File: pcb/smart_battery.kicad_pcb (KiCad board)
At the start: 2 copper layers, 109.2 x 108 mm, 37 parts, among them J11 Conn_01x05_RTC, J12 Conn_HtrTh, J13 Conn_BattTh, Q1 MMBT5551L, Q2 MMBT5551L, U1 SPX3819M5-L-3-3, U10 FEATHER_M0_ADALOGGER, U11 FEATHERWING_HEATER_RELAY, U12 FEATHERWING_ETHERNET, U13 FEATHERWING_MINI_RELAY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

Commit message: Routed the new layout just need ground plane
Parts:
- added C5: C10uF, Capacitor_SMD:C_0805_2012Metric, B.Cu at (109.2, 74.9)
- added C6: C10uF, Capacitor_SMD:C_0805_2012Metric, B.Cu at (110.5, 90.2)
- added C7: C10uF, Capacitor_SMD:C_0805_2012Metric, B.Cu at (110.5, 92.7)
- added C8: C10nF, Capacitor_SMD:C_0805_2012Metric, B.Cu at (85.1, 30.5)
- added F1: Fuse_Small, Fuse:Fuseholder_Cylinder-5x20mm_Schurter_0031_8201_Horizontal_Open, B.Cu at (55.9, 82.5)
- added F2: Fuse_Small, Fuse:Fuseholder_Cylinder-5x20mm_Schurter_0031_8201_Horizontal_Open, B.Cu at (34.3, 55.9)
- added R10: 3.3K, Resistor_SMD:R_0805_2012Metric, B.Cu at (101.6, 52.1)
- added R11: R6.8k, Resistor_SMD:R_0805_2012Metric, B.Cu at (101.6, 54.6)
- added R12: 3.3K, Resistor_SMD:R_0805_2012Metric, B.Cu at (109.2, 72.4)
- added R13: R6.8k, Resistor_SMD:R_0805_2012Metric, B.Cu at (101.6, 95.2)
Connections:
- net /BATPWR renamed Net-(D1-Pad2)
- net /SOLPWR renamed Net-(D2-Pad2)
- C1 pad 1: /POUT -> +48V
- C2 pad 1: /Eth3.3 -> +48V
- C3 pad 1: /Eth3.3 -> +48V
- D1 pad 1: /DBPWR -> Net-(D1-Pad1)
- PS1 pad 1: Net-(D2-Pad1) -> +48V
- PS2 pad 2: /DBPWR -> +48V
- Q1 pad 3: /DBPWR -> +48V
- R5 pad 2: /POUT -> +48V
- R6 pad 1: /DBPWR -> +48V
- U1 pad 1: /POUT -> +48V
- U1 pad 5: /Eth3.3 -> +48V
- U12 pad P1_15: /Eth3.3 -> +48V
- U13 pad P1_1: GND -> Net-(U13-PadP1_1)
- U13 pad P1_13: GND -> Net-(U13-PadP1_1)
- U14 pad P2_2: /POUT -> +48V
- U1Batt1 pad 9: GND -> Net-(R12-Pad1)
- U2Solar1 pad 9: GND -> Net-(R10-Pad1)
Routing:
- net +48V: track 22.0 -> 274.3 mm
- net GND: track 551.9 -> 460.1 mm, vias 0 -> 7
- net /POUT: track 47.5 -> 0.00 mm, vias 1 -> 0
- net Net-(R12-Pad1): track 0.00 -> 39.2 mm
- net Net-(U13-PadP1_1): track 0.00 -> 36.4 mm
- net Net-(D1-Pad1): track 0.00 -> 32.6 mm
- net Net-(D2-Pad1): track 16.2 -> 46.5 mm
- net /DBPWR: track 27.2 -> 0.00 mm
- net /Eth3.3: track 19.2 -> 0.00 mm
- net /ENCS: track 119.3 -> 105.0 mm, vias 0 -> 1
- net Net-(R10-Pad1): track 0.00 -> 11.0 mm
- net +5V: track 195.5 -> 206.4 mm, vias 0 -> 1
- net Net-(D1-Pad2): track 49.0 -> 57.6 mm
- net /SUSET: track 43.2 -> 51.1 mm
- net /~RST: track 138.0 -> 144.7 mm
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- removed copper zone on F.Cu, net GND

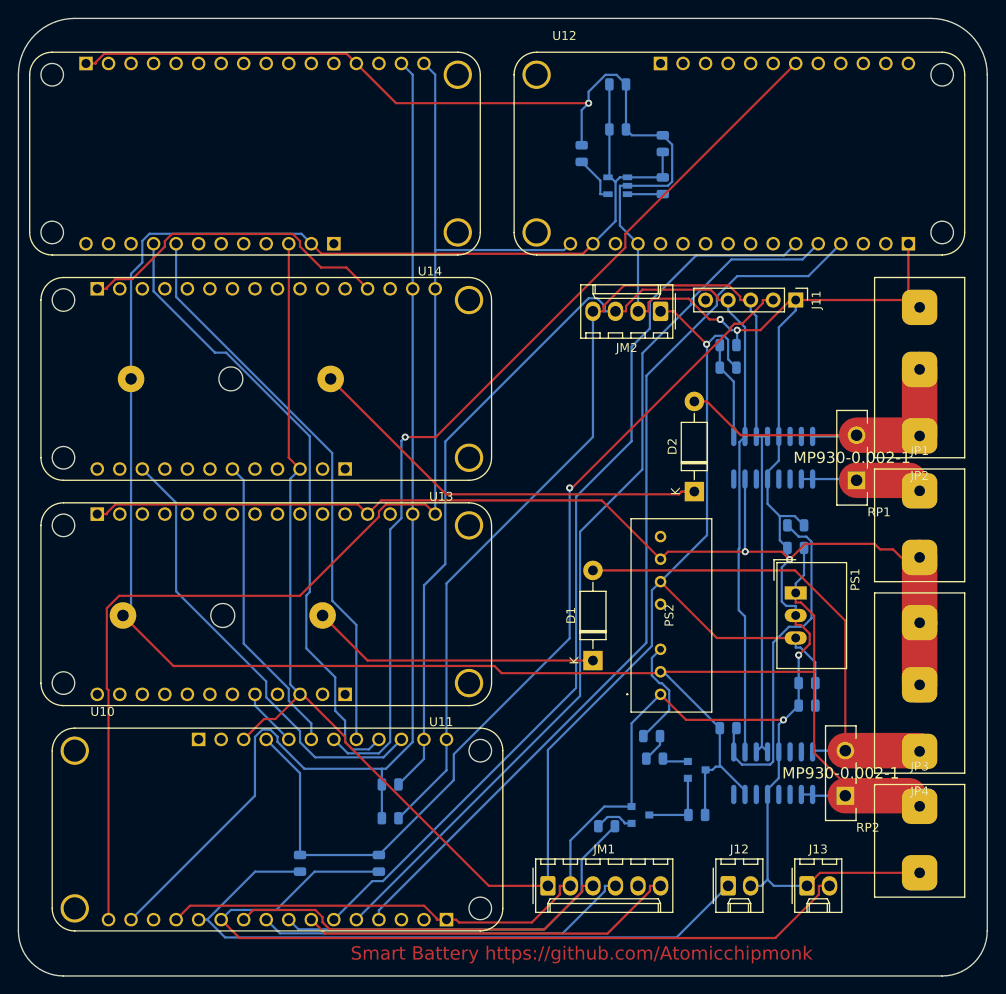
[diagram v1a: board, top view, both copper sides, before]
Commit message: Made the ground plane
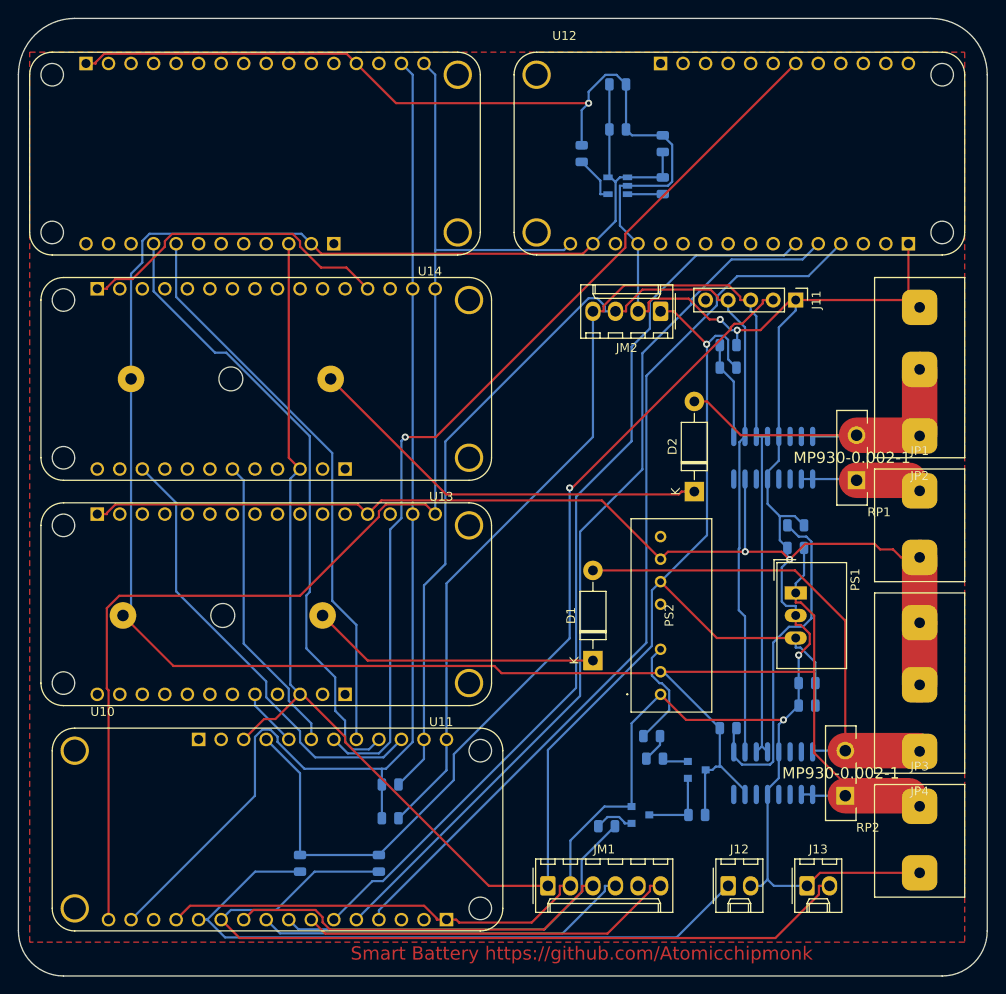
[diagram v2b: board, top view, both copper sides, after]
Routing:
- added copper zone on F.Cu, net GND
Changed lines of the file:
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@@
   (segment (start 32.5242 70.0297) (end 31.5703 70.9836) (width 0.25) (layer F.Cu) (net 3))
   (segment (start 31.5703 70.9836) (end 31.5703 71.12) (width 0.25) (layer F.Cu) (net 3))
-  (via (at 85.8712 24.7962) (size 0.8) (layers F.Cu B.Cu) (net 3))
+  (via (at 85.8712 24.7962) (size 0.8) (layers F.Cu B.Cu) (net 3) (status 1000000))
   (via (at 107.8404 94.3212) (size 0.8) (layers F.Cu B.Cu) (net 3))
   (via (at 100.7078 49.1765) (size 0.8) (layers F.Cu B.Cu) (net 3))
@@
   (segment (start 86.36 87.63) (end 60.96 87.63) (width 0.25) (layer F.Cu) (net 142))
   (segment (start 60.96 87.63) (end 55.88 82.55) (width 0.25) (layer F.Cu) (net 142))
+  (zone (net 3) (net_name GND) (layer F.Cu) (hatch edge 0.508)
+    (connect_pads (clearance 0.508))
+    (min_thickness 0.254)
+    (fill yes (arc_segments 16) (thermal_gap 0.508) (thermal_bridge_width 0.508))
+    (polygon
+      (pts
+        (xy 22.86 19.05) (xy 128.27 19.05) (xy 128.27 119.38) (xy 22.86 119.38) (xy 22.86 118.11)
+      )
+    )
+  )
 )
